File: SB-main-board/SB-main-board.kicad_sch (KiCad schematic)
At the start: 88 parts, among them J1 XT30PB_IN, J2 USB_C_Receptacle_USB2.0_16P, J3 Excluder, J4 PT100, J5 Hotend, J6 FAN2, J7 LDC, J8 FS, J9 FAN, Q1 BUK9M8R5-40EX, SW1 BOOT, U1 RP2040, U10 TMP235A2, U2 W25Q16JVUXIQ, U3 TJA1042TK-3, U4 TPS560430YF, U5 LP5912-3.3DRV, U6 TMC2208-LA, U7 OR, U8 LIS2DW12, U9 MAX31865xTP, Y1 12MHz

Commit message: change bom
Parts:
- Q1: value BUK9M8R5-40EX -> BUK9M4R3-40H
- R15: value 11mR -> 200mR
- R16: value 11mR -> 220mR
- U10: value TMP235A2 -> LM50
- U6: value TMC2208-LA -> TMC2209-LA
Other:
- moved on the sheet: R15, R16
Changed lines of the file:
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@@
 	)
 	(junction
+		(at 205.74 87.63)
+		(diameter 0)
+		(color 0 0 0 0)
+	)
+	(junction
 		(at 274.32 34.29)
 		(diameter 0)
@@
 	)
 	(junction
-		(at 273.05 170.18)
+		(at 223.52 97.79)
 		(diameter 0)
 		(color 0 0 0 0)
 	)
 	(junction
-		(at 104.14 259.08)
+		(at 273.05 170.18)
 		(diameter 0)
 		(color 0 0 0 0)
 	)
 	(junction
-		(at 214.63 97.79)
+		(at 104.14 259.08)
 		(diameter 0)
 		(color 0 0 0 0)
@@
 	)
 	(junction
-		(at 207.01 87.63)
-		(diameter 0)
-		(color 0 0 0 0)
-	)
-	(junction
 		(at 177.8 124.46)
 		(diameter 0)
@@
 	)
 	(junction
+		(at 214.63 97.79)
+		(diameter 0)
+		(color 0 0 0 0)
+	)
+	(junction
 		(at 200.66 198.12)
 		(diameter 0)
@@
 	)
 	(junction
-		(at 224.79 97.79)
-		(diameter 0)
-		(color 0 0 0 0)
-	)
-	(junction
 		(at 27.94 67.31)
 		(diameter 0)
@@
 	)
 	(junction
-		(at 224.79 85.09)
+		(at 27.94 83.82)
 		(diameter 0)
 		(color 0 0 0 0)
 	)
 	(junction
-		(at 27.94 83.82)
+		(at 172.72 77.47)
 		(diameter 0)
 		(color 0 0 0 0)
 	)
 	(junction
-		(at 172.72 77.47)
+		(at 201.93 214.63)
 		(diameter 0)
 		(color 0 0 0 0)
 	)
 	(junction
-		(at 201.93 214.63)
+		(at 223.52 85.09)
 		(diameter 0)
 		(color 0 0 0 0)
@@
 	(wire
 		(pts
-			(xy 219.71 97.79) (xy 224.79 97.79)
+			(xy 219.71 97.79) (xy 223.52 97.79)
 		)
 		(stroke
@@
 	(wire
 		(pts
-			(xy 224.79 85.09) (xy 224.79 90.17)
+			(xy 223.52 85.09) (xy 223.52 90.17)
 		)
 		(stroke
@@
 	(wire
 		(pts
-			(xy 207.01 95.25) (xy 207.01 97.79)
+			(xy 205.74 95.25) (xy 205.74 97.79)
 		)
 		(stroke
@@
 	(wire
 		(pts
-			(xy 224.79 95.25) (xy 224.79 97.79)
+			(xy 223.52 95.25) (xy 223.52 97.79)
 		)
 		(stroke
@@
 	(wire
 		(pts
-			(xy 207.01 87.63) (xy 207.01 90.17)
+			(xy 205.74 87.63) (xy 205.74 90.17)
 		)
 		(stroke
@@
 	(wire
 		(pts
-			(xy 204.47 87.63) (xy 207.01 87.63)
+			(xy 204.47 87.63) (xy 205.74 87.63)
 		)
 		(stroke
@@
 	(wire
 		(pts
+			(xy 205.74 87.63) (xy 214.63 87.63)
+		)
+		(stroke
+			(width 0)
+			(type default)
+		)
+	)
+	(wire
+		(pts
 			(xy 186.69 173.99) (xy 186.69 175.26)
 		)
@@
 	(wire
 		(pts
+			(xy 223.52 85.09) (xy 232.41 85.09)
+		)
+		(stroke
+			(width 0)
+			(type default)
+		)
+	)
+	(wire
+		(pts
 			(xy 128.27 58.42) (xy 138.43 58.42)
 		)
@@
 	(wire
 		(pts
-			(xy 214.63 97.79) (xy 219.71 97.79)
-		)
-		(stroke
-			(width 0)
-			(type default)
-		)
-	)
-	(wire
-		(pts
 			(xy 214.63 95.25) (xy 214.63 97.79)
 		)
@@
 	(wire
 		(pts
+			(xy 214.63 97.79) (xy 219.71 97.79)
+		)
+		(stroke
+			(width 0)
+			(type default)
+		)
+	)
+	(wire
+		(pts
 			(xy 207.01 207.01) (xy 207.01 205.74)
 		)
@@
 	(wire
 		(pts
+			(xy 223.52 97.79) (xy 232.41 97.79)
+		)
+		(stroke
+			(width 0)
+			(type default)
+		)
+	)
+	(wire
+		(pts
 			(xy 57.15 212.09) (xy 72.39 212.09)
 		)
@@
 	(wire
 		(pts
-			(xy 207.01 97.79) (xy 214.63 97.79)
+			(xy 205.74 97.79) (xy 214.63 97.79)
 		)
 		(stroke
@@
 	(wire
 		(pts
-			(xy 204.47 85.09) (xy 224.79 85.09)
+			(xy 204.47 85.09) (xy 223.52 85.09)
 		)
 		(stroke
@@
 	(wire
 		(pts
-			(xy 232.41 85.09) (xy 224.79 85.09)
-		)
-		(stroke
-			(width 0)
-			(type default)
-		)
-	)
-	(wire
-		(pts
 			(xy 177.8 124.46) (xy 182.88 124.46)
 		)
@@
 	(wire
 		(pts
-			(xy 214.63 87.63) (xy 207.01 87.63)
-		)
-		(stroke
-			(width 0)
-			(type default)
-		)
-	)
-	(wire
-		(pts
 			(xy 87.63 127) (xy 87.63 128.27)
 		)
@@
 	(wire
 		(pts
-			(xy 224.79 97.79) (xy 232.41 97.79)
-		)
-		(stroke
-			(width 0)
-			(type default)
-		)
-	)
-	(wire
-		(pts
 			(xy 177.8 26.67) (xy 177.8 25.4)
 		)
@@
 			)
 		)
-		(property "Value" "BUK9M8R5-40EX"
+		(property "Value" "BUK9M4R3-40H"
 			(at 278.13 41.9099 0)
 			(effects
@@
 	(symbol
 		(lib_id "Device:R_Small_US")
-		(at 224.79 92.71 0)
+		(at 223.52 92.71 0)
 		(mirror y)
 		(unit 1)
@@
 		(dnp no)
 		(property "Reference" "R16"
-			(at 226.06 91.44 0)
+			(at 224.79 91.44 0)
 			(effects
 				(font
@@
 			)
 		)
-		(property "Value" "11mR"
-			(at 226.06 93.98 0)
+		(property "Value" "220mR"
+			(at 224.79 93.98 0)
 			(effects
 				(font
@@
 		)
 		(property "Footprint" "Resistor_SMD:R_0805_2012Metric"
-			(at 224.79 92.71 0)
+			(at 223.52 92.71 0)
 			(effects
 				(font
@@
 		)
 		(property "Datasheet" "~"
-			(at 224.79 92.71 0)
+			(at 223.52 92.71 0)
 			(effects
 				(font
@@
 		)
 		(property "Description" "Resistor, small US symbol"
-			(at 224.79 92.71 0)
+			(at 223.52 92.71 0)
 			(effects
 				(font
@@
 	(symbol
 		(lib_id "Device:R_Small_US")
-		(at 207.01 92.71 0)
+		(at 205.74 92.71 0)
 		(mirror y)
 		(unit 1)
@@
 		(dnp no)
 		(property "Reference" "R15"
-			(at 208.28 91.44 0)
+			(at 207.01 91.44 0)
 			(effects
 				(font
@@
 			)
 		)
-		(property "Value" "11mR"
-			(at 208.28 93.98 0)
+		(property "Value" "200mR"
+			(at 207.01 93.98 0)
 			(effects
 				(font
@@
 		)
 		(property "Footprint" "Resistor_SMD:R_0805_2012Metric"
-			(at 207.01 92.71 0)
+			(at 205.74 92.71 0)
 			(effects
 				(font
@@
 		)
 		(property "Datasheet" "~"
-			(at 207.01 92.71 0)
+			(at 205.74 92.71 0)
 			(effects
 				(font
@@
 		)
 		(property "Description" "Resistor, small US symbol"
-			(at 207.01 92.71 0)
+			(at 205.74 92.71 0)
 			(effects
 				(font
@@
 		(on_board yes)
 		(dnp no)
-		(fields_autoplaced yes)
 		(property "Reference" "U6"
-			(at 191.4241 36.83 0)
+			(at 190.5 93.98 0)
 			(effects
 				(font
@@
 			)
 		)
-		(property "Value" "TMC2208-LA"
-			(at 191.4241 39.37 0)
+		(property "Value" "TMC2209-LA"
+			(at 190.5 96.52 0)
 			(effects
 				(font
@@
 			)
 		)
-		(property "Value" "TMP235A2"
+		(property "Value" "LM50"
 			(at 185.42 264.1599 0)
 			(effects

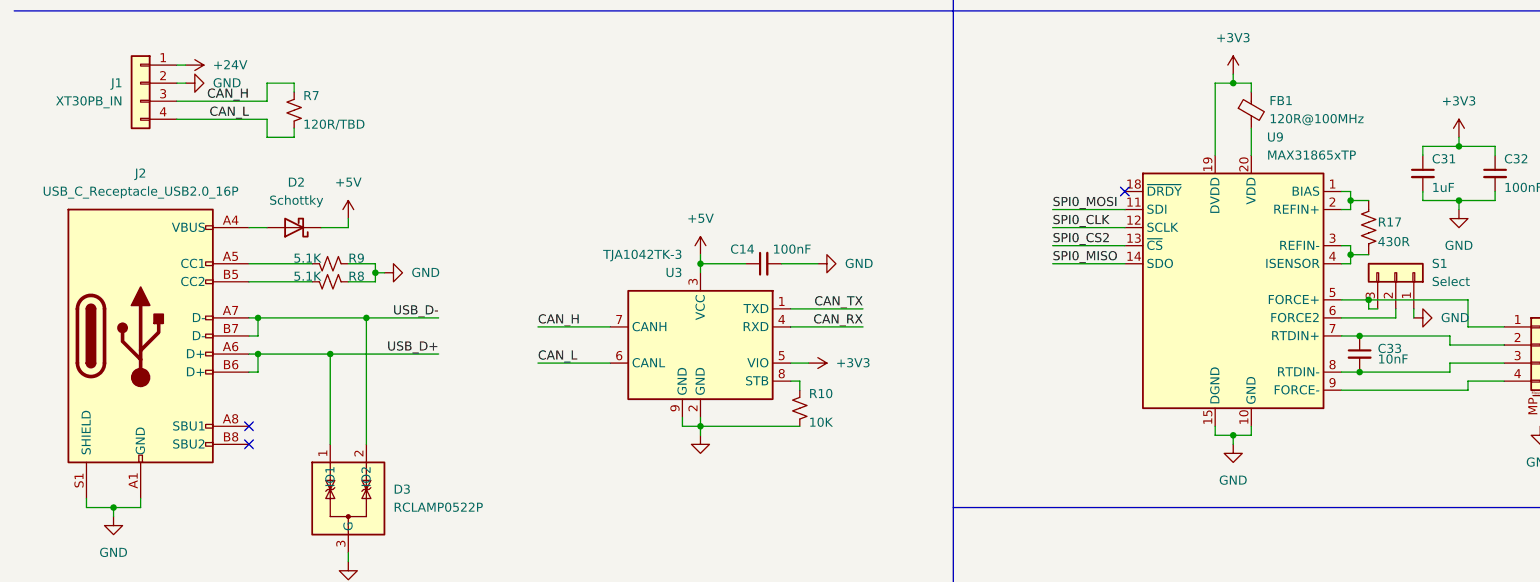
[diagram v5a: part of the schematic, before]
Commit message: layout: optmise routes
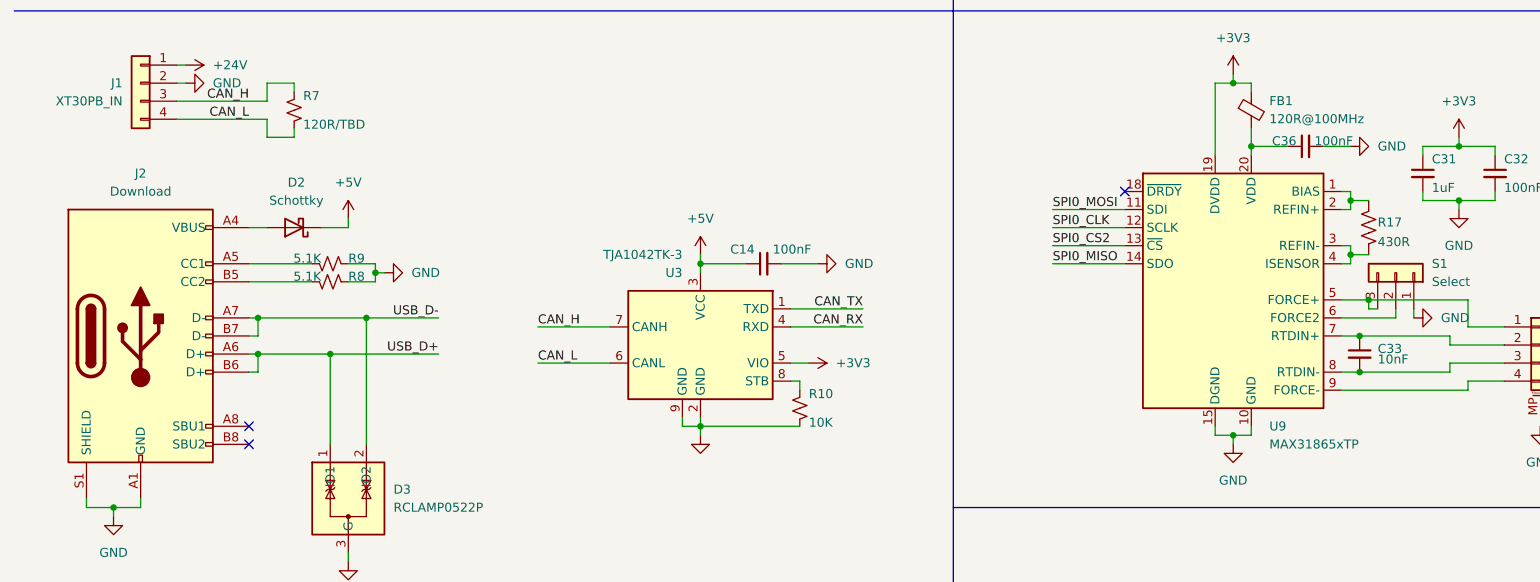
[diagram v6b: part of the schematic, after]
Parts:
- added C36: 100nF, Capacitor_SMD:C_0402_1005Metric, symbol Device:C_Small
- J2: value USB_C_Receptacle_USB2.0_16P -> Download
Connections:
- net GND: now also C36.2
- net at FB1.2, U9.20 (VDD): now also C36.1
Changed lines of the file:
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@@
 	)
 	(junction
+		(at 186.69 182.88)
+		(diameter 0)
+		(color 0 0 0 0)
+	)
+	(junction
 		(at 172.72 77.47)
 		(diameter 0)
@@
 	(wire
 		(pts
+			(xy 186.69 182.88) (xy 191.77 182.88)
+		)
+		(stroke
+			(width 0)
+			(type default)
+		)
+	)
+	(wire
+		(pts
 			(xy 167.64 25.4) (xy 177.8 25.4)
 		)
@@
 	(wire
 		(pts
+			(xy 196.85 182.88) (xy 200.66 182.88)
+		)
+		(stroke
+			(width 0)
+			(type default)
+		)
+	)
+	(wire
+		(pts
 			(xy 121.92 205.74) (xy 132.08 205.74)
 		)
@@
 	(wire
 		(pts
-			(xy 186.69 180.34) (xy 186.69 184.15)
+			(xy 186.69 180.34) (xy 186.69 182.88)
 		)
 		(stroke
@@
 	(wire
 		(pts
+			(xy 186.69 182.88) (xy 186.69 184.15)
+		)
+		(stroke
+			(width 0)
+			(type default)
+		)
+	)
+	(wire
+		(pts
 			(xy 264.16 24.13) (xy 262.89 24.13)
 		)
@@
 		(on_board yes)
 		(dnp no)
-		(fields_autoplaced yes)
 		(property "Reference" "U9"
-			(at 188.8841 181.61 0)
+			(at 189.23 222.25 0)
 			(effects
 				(font
@@
 		)
 		(property "Value" "MAX31865xTP"
-			(at 188.8841 184.15 0)
+			(at 189.23 224.79 0)
 			(effects
 				(font
@@
 			)
 		)
-		(property "Value" "USB_C_Receptacle_USB2.0_16P"
+		(property "Value" "Download"
 			(at 30.48 189.23 0)
 			(effects
@@
 	(symbol
 		(lib_id "power:GND")
+		(at 200.66 182.88 90)
+		(unit 1)
+		(exclude_from_sim no)
+		(in_bom yes)
+		(on_board yes)
+		(dnp no)
+		(fields_autoplaced yes)
+		(property "Reference" "#PWR015"
+			(at 207.01 182.88 0)
+			(effects
+				(font
+					(size 1.27 1.27)
+				)
+				(hide yes)
+			)
+		)
+		(property "Value" "GND"
+			(at 204.47 182.8799 90)
+			(effects
+				(font
+					(size 1.27 1.27)
+				)
+				(justify right)
+			)
+		)
+		(property "Footprint" ""
+			(at 200.66 182.88 0)
+			(effects
+				(font
+					(size 1.27 1.27)
+				)
+				(hide yes)
+			)
+		)
+		(property "Datasheet" ""
+			(at 200.66 182.88 0)
+			(effects
+				(font
+					(size 1.27 1.27)
+				)
+				(hide yes)
+			)
+		)
+		(property "Description" "Power symbol creates a global label with name \"GND\" , ground"
+			(at 200.66 182.88 0)
+			(effects
+				(font
+					(size 1.27 1.27)
+				)
+				(hide yes)
+			)
+		)
+		(pin "1"
+		)
+		(instances
+			(project "SB-main-board"
+				(path "/e3d9bf3f-f8be-4a0d-9b69-f1016d65a8ba"
+					(reference "#PWR015")
+					(unit 1)
+				)
+			)
+		)
+	)
+	(symbol
+		(lib_id "power:GND")
 		(at 102.87 156.21 0)
 		(unit 1)
@@
 					(unit 1)
 				)
+			)
+		)
+	)
+	(symbol
+		(lib_id "Device:C_Small")
+		(at 194.31 182.88 90)
+		(unit 1)
+		(exclude_from_sim no)
+		(in_bom yes)
+		(on_board yes)
+		(dnp no)
+		(property "Reference" "C36"
+			(at 193.04 182.88 90)
+			(effects
+				(font
+					(size 1.27 1.27)
+				)
+				(justify left top)
+			)
+		)
+		(property "Value" "100nF"
+			(at 195.58 182.88 90)
+			(effects
+				(font
+					(size 1.27 1.27)
+				)
+				(justify right top)
+			)
+		)
+		(property "Footprint" "Capacitor_SMD:C_0402_1005Metric"
+			(at 194.31 182.88 0)
+			(effects
+				(font
+					(size 1.27 1.27)
+				)
+				(hide yes)
+			)
+		)
+		(property "Datasheet" "~"
+			(at 194.31 182.88 0)
+			(effects
+				(font
+					(size 1.27 1.27)
+				)
+				(hide yes)
+			)
+		)
+		(property "Description" "Unpolarized capacitor, small symbol"
+			(at 194.31 182.88 0)
+			(effects
+				(font
+					(size 1.27 1.27)
+				)
+				(hide yes)
+			)
+		)
+		(pin "1"
+		)
+		(pin "2"
+		)
+		(instances
+			(project "SB-main-board"
+				(path "/e3d9bf3f-f8be-4a0d-9b69-f1016d65a8ba"
+					(reference "C36")
+					(unit 1)
+				)

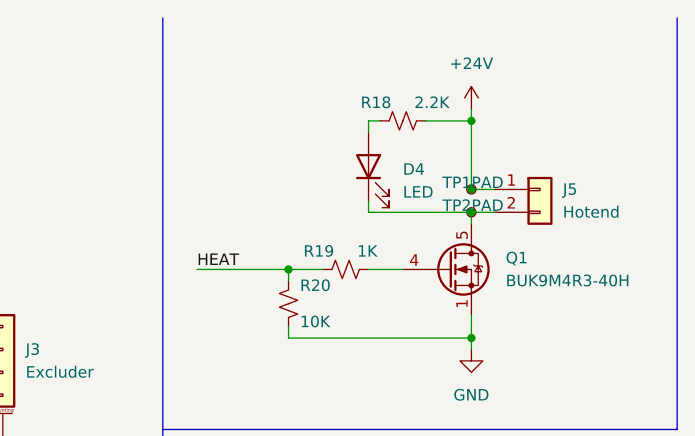
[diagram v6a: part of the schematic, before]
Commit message: layout: swap the led and the resistor
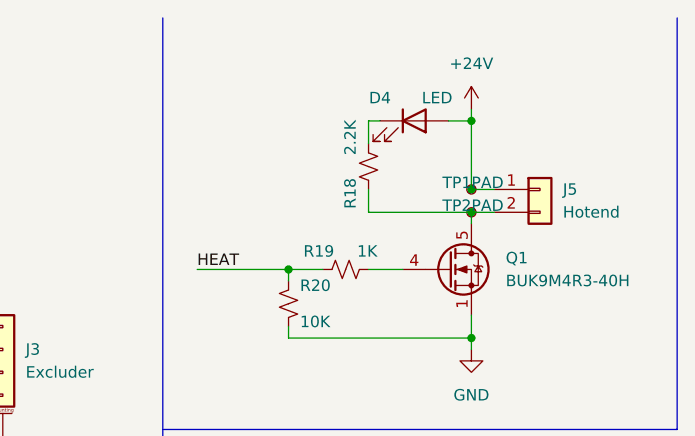
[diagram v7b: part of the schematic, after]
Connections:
- net +24V: now also D4.2 (A); no longer R18.2
- net at J5.2 (Pin_2), Q1.5 (D), TP2.1: now also R18.1; no longer D4.1 (K)
- new net: D4.1 (K), R18.2
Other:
- moved on the sheet: D4, R18
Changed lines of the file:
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@@
 	(wire
 		(pts
-			(xy 262.89 24.13) (xy 262.89 25.4)
-		)
-		(stroke
-			(width 0)
-			(type default)
-		)
-	)
-	(wire
-		(pts
 			(xy 67.31 40.64) (xy 77.47 40.64)
 		)
@@
 	(wire
 		(pts
+			(xy 271.78 24.13) (xy 274.32 24.13)
+		)
+		(stroke
+			(width 0)
+			(type default)
+		)
+	)
+	(wire
+		(pts
 			(xy 45.72 212.09) (xy 46.99 212.09)
 		)
@@
 	(wire
 		(pts
-			(xy 262.89 34.29) (xy 262.89 33.02)
+			(xy 262.89 31.75) (xy 262.89 34.29)
 		)
 		(stroke
@@
 	(wire
 		(pts
-			(xy 269.24 24.13) (xy 274.32 24.13)
-		)
-		(stroke
-			(width 0)
-			(type default)
-		)
-	)
-	(wire
-		(pts
 			(xy 173.99 46.99) (xy 172.72 46.99)
 		)
@@
 	(wire
 		(pts
+			(xy 262.89 24.13) (xy 262.89 26.67)
+		)
+		(stroke
+			(width 0)
+			(type default)
+		)
+	)
+	(wire
+		(pts
 			(xy 77.47 261.62) (xy 77.47 259.08)
 		)
@@
 	(symbol
 		(lib_id "Device:LED")
-		(at 262.89 29.21 90)
+		(at 267.97 24.13 0)
 		(unit 1)
 		(exclude_from_sim no)
@@
 		(on_board yes)
 		(dnp no)
-		(fields_autoplaced yes)
 		(property "Reference" "D4"
-			(at 266.7 29.5274 90)
+			(at 264.16 21.59 0)
 			(effects
 				(font
 					(size 1.27 1.27)
 				)
-				(justify right)
 			)
 		)
 		(property "Value" "LED"
-			(at 266.7 32.0674 90)
+			(at 270.51 21.59 0)
 			(effects
 				(font
 					(size 1.27 1.27)
 				)
-				(justify right)
 			)
 		)
 		(property "Footprint" "LED_SMD:LED_0402_1005Metric"
-			(at 262.89 29.21 0)
+			(at 267.97 24.13 0)
 			(effects
 				(font
@@
 		)
 		(property "Datasheet" "~"
-			(at 262.89 29.21 0)
+			(at 267.97 24.13 0)
 			(effects
 				(font
@@
 		)
 		(property "Description" "Light emitting diode"
-			(at 262.89 29.21 0)
+			(at 267.97 24.13 0)
 			(effects
 				(font
@@
 	(symbol
 		(lib_id "Device:R_Small_US")
-		(at 266.7 24.13 90)
+		(at 262.89 29.21 180)
 		(unit 1)
 		(exclude_from_sim no)
@@
 		(dnp no)
 		(property "Reference" "R18"
-			(at 265.43 22.86 90)
+			(at 261.62 30.48 90)
 			(effects
 				(font
@@
 		)
 		(property "Value" "2.2K"
-			(at 267.97 22.86 90)
+			(at 261.62 27.94 90)
 			(effects
 				(font
@@
 		)
 		(property "Footprint" "Resistor_SMD:R_0402_1005Metric"
-			(at 266.7 24.13 0)
+			(at 262.89 29.21 0)
 			(effects
 				(font
@@
 		)
 		(property "Datasheet" "~"
-			(at 266.7 24.13 0)
+			(at 262.89 29.21 0)
 			(effects
 				(font
@@
 		)
 		(property "Description" "Resistor, small US symbol"
-			(at 266.7 24.13 0)
+			(at 262.89 29.21 0)
 			(effects
 				(font

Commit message: footprint: change input cap to 1206
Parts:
- C16: footprint Capacitor_SMD:C_0805_2012Metric -> Capacitor_SMD:C_1206_3216Metric
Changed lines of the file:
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@@
 			)
 		)
-		(property "Footprint" "Capacitor_SMD:C_0805_2012Metric"
+		(property "Footprint" "Capacitor_SMD:C_1206_3216Metric"
 			(at 20.32 265.43 0)
 			(effects
